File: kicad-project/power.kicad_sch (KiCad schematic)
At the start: 18 parts

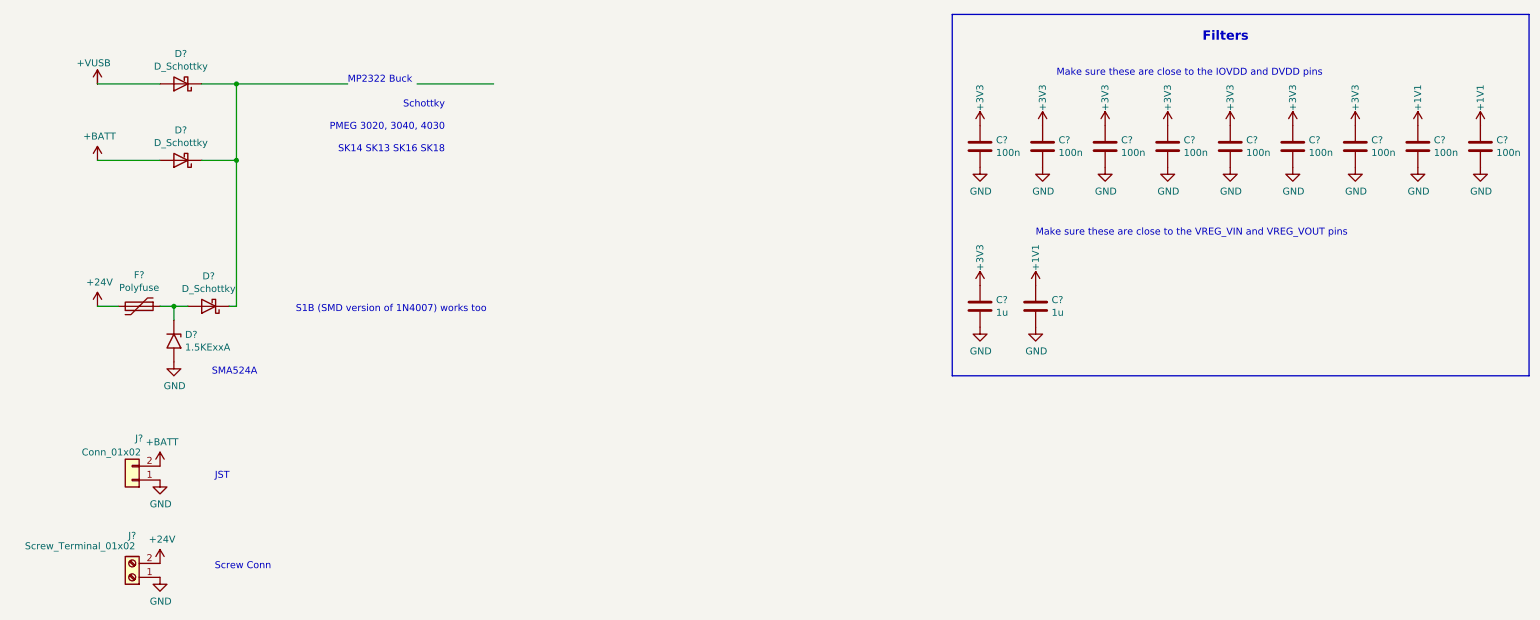
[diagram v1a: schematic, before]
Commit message: hw: add flash, switching circuit and XOUT resistor, change GPS and general cleanup
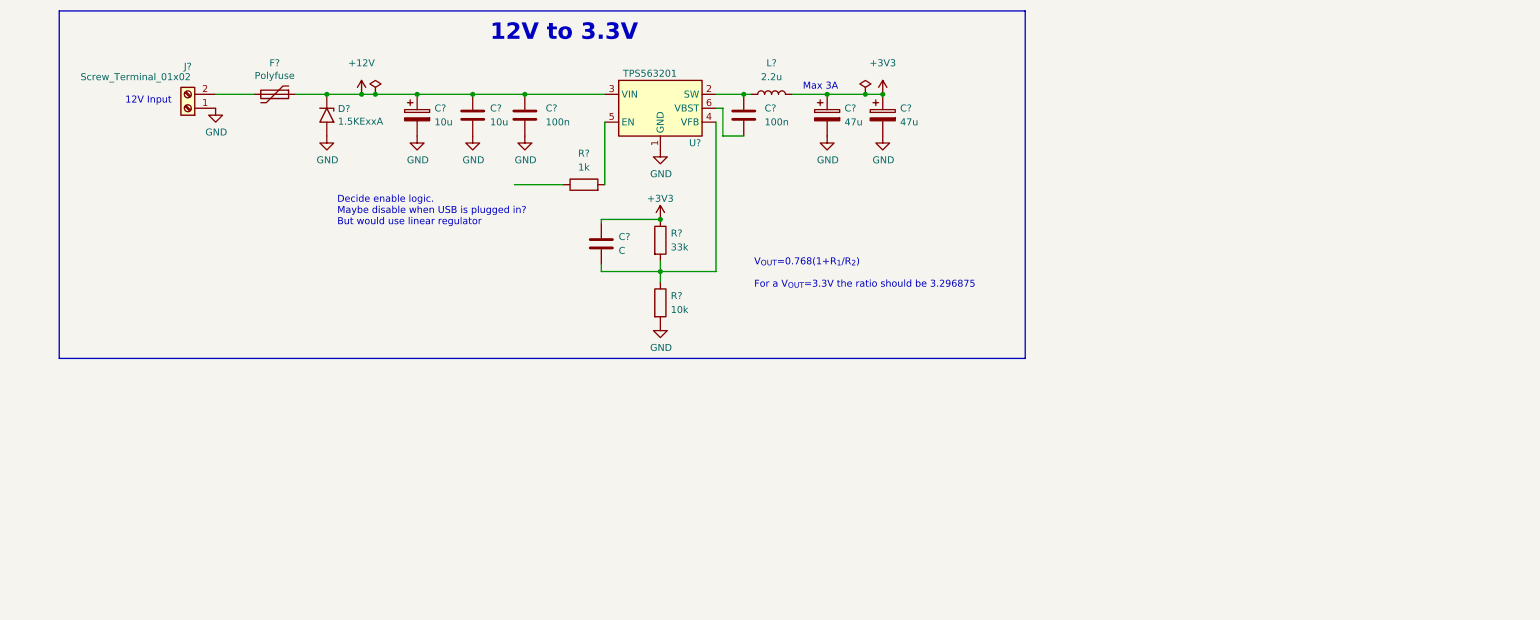
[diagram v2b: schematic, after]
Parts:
- removed C? (x9): 100n, Capacitor_SMD:C_0603_1608Metric, symbol Device:C
- removed C? (x2): 1u, Capacitor_SMD:C_0603_1608Metric, symbol Device:C
- removed D? (x3): D_Schottky, symbol Device:D_Schottky
- removed J?: Conn_01x02, symbol Connector_Generic:Conn_01x02
- added C?: 10u, symbol Device:C_Polarized
- added C?: C, symbol Device:C
- added C? (x2): 47u, symbol Device:C_Polarized
- added C? (x2): 100n, symbol Device:C
- added C?: 10u, symbol Device:C
- added L?: 2.2u, symbol Device:L
- added R?: 33k, symbol Device:R
- added R?: 10k, symbol Device:R
- added R?: 1k, symbol Device:R
- added U?: TPS563201, Package_TO_SOT_SMD:SOT-23-6, symbol Regulator_Switching:TPS563200
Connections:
- net +3V3: now also C?.1, C?.1, C?.1, L?.2, R?.1
- net GND: now also C?.2, C?.2, C?.2, C?.2, C?.2, R?.2, U?.1 (GND)
- net +12V: now reaches D?.1 (A1), F?.1
- net +12V: now also C?.1, C?.1, C?.1, U?.3 (VIN)
- net +24V: no longer names the net of F?.2, J?.2 (Pin_2)
- new net: C?.2, R?.1, R?.2, U?.4 (VFB)
- new net: C?.1, L?.1, U?.2 (SW)
- new net: R?.2, U?.5 (EN)
- new net: C?.2, U?.6 (VBST)
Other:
- note added: "12V Input"
- note added: "12V to 3.3V"
- note added: "Decide enable logic. Maybe disable when USB is plugged in? But would use linear regulator"
- note added: "Max 3A"
- note added: "V_{OUT}=0.768(1+R_{1}/R_{2}) For a V_{OUT}=3.3V the ratio should be 3.296875"
- note removed: "Filters"
- note removed: "JST"
- note removed: "MP2322 Buck"
- note removed: "Make sure these are close to the IOVDD and DVDD pins"
- note removed: "Make sure these are close to the VREG_VIN and VREG_VOUT pins"
- note removed: "S1B (SMD version of 1N4007) works too"
- note removed: "SMA524A"
- note removed: "Schottky PMEG 3020, 3040, 4030 SK14 SK13 SK16 SK18"
- note removed: "Screw Conn"
- title: (none) -> Power
- moved on the sheet: D?, F?, J?

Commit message: hw: add limit switches, dual power input, actuation sheet, debug and expansion connectors and connect sheets
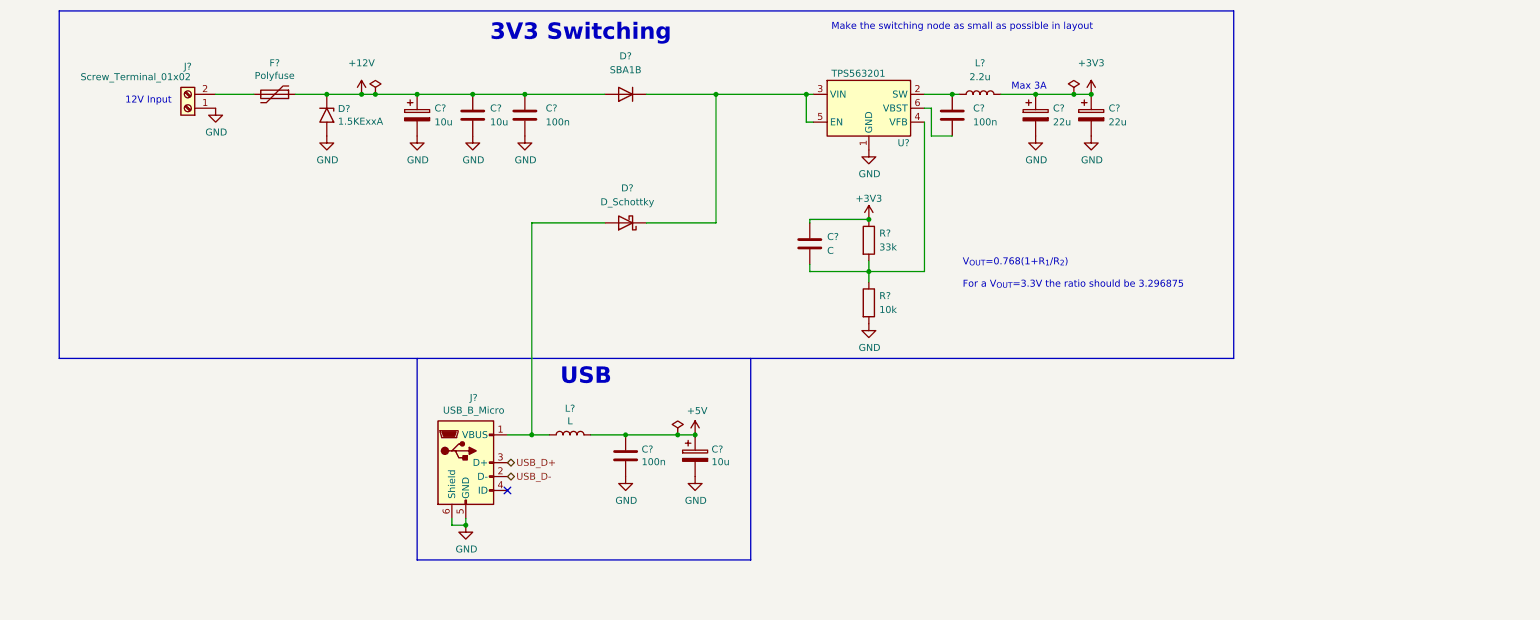
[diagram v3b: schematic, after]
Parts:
- removed R?: 1k, symbol Device:R
- added C?: 10u, symbol Device:CP
- added C?: 100n, symbol Device:C
- added D?: SBA1B, symbol Diode:1N4007
- added D?: D_Schottky, symbol Device:D_Schottky
- added J?: USB_B_Micro, symbol Connector:USB_B_Micro
- added L?: L, symbol Device:L
- C? (x2): value 47u -> 22u
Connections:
- net +12V: now also D?.2 (A); no longer U?.3 (VIN)
- net GND: now also C?.2, C?.2, J?.5 (GND), J?.6 (Shield)
- net at U?.5 (EN): now also U?.3 (VIN), D?.1 (K), D?.1 (K)
- new net: D?.2 (A), J?.1 (VBUS), L?.1
- new net +5V: C?.1, C?.1, L?.2
- new net USB_D+: J?.3 (D+)
- new net USB_D-: J?.2 (D-)
- no-connect marks 0 -> 1
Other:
- note added: "3V3 Switching"
- note added: "Make the switching node as small as possible in layout"
- note added: "USB"
- note removed: "12V to 3.3V"
- note removed: "Decide enable logic. Maybe disable when USB is plugged in? But would use linear regulator"
- moved on the sheet: C?, L?, R?, U?

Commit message: hw: schematic updates
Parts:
- removed C?: 10u, symbol Device:C
- added C? (x2): 10u, symbol Device:C_Polarized
- D?: value D_Schottky -> (none)
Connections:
- net +12V: now also C?.1
- net +5V: now also C?.1
- net GND: now also C?.2, C?.2
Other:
- note added: "How about no R in EN? 10k"
- note added: "S: Why not molex?"
- note added: "Why TVS here? Assuming 4x4.2 full charged LiPo/Li-Ion the diode should have 16.8V working voltage. We haven't found any TVS 16.8V."
- note added: "need motor current"
- note added: "perche 10 u polarizzati?"
- moved on the sheet: C?, D?, F?, J?, L?, R?, U?

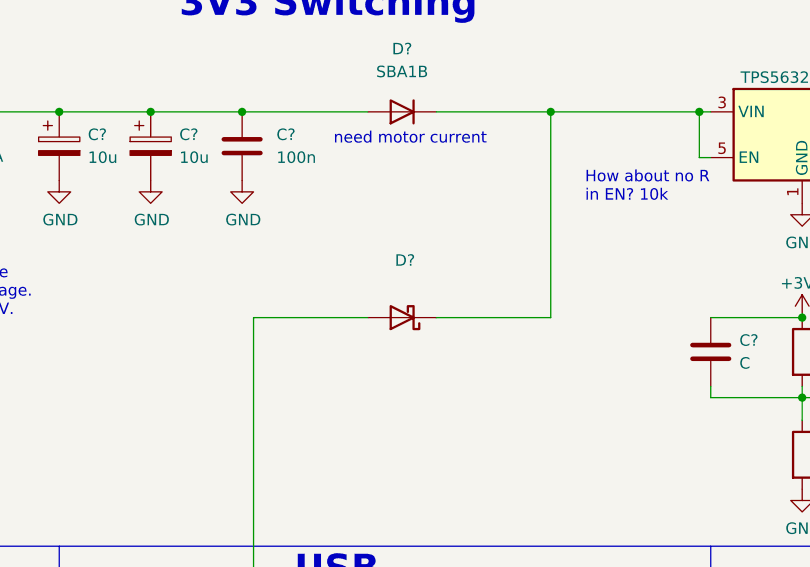
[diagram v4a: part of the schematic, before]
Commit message: hw: connect filtering capacitor near vdd pin
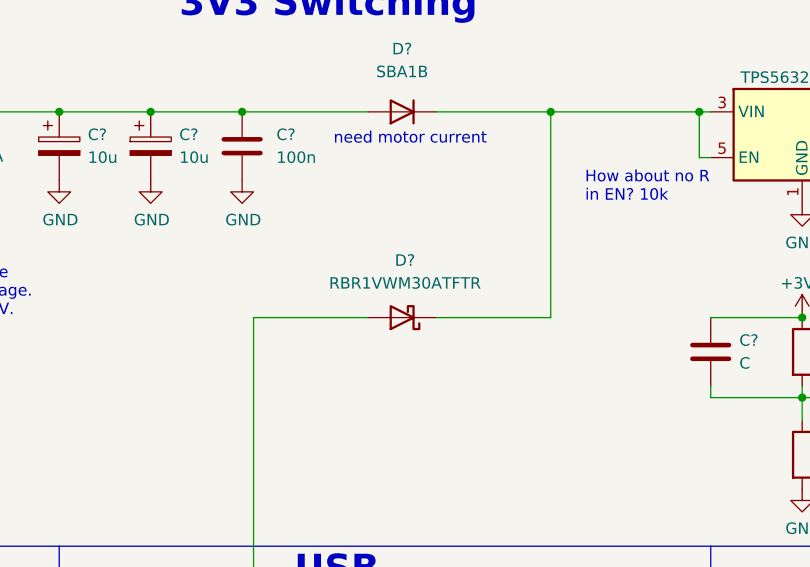
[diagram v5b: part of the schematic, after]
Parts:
- D?: value (none) -> RBR1VWM30ATFTR
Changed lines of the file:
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@@
     (in_bom yes) (on_board yes) (fields_autoplaced)
     (property "Reference" "D?" (id 0) (at 117.1575 45.72 0))
-    (property "Value" "" (id 1) (at 117.1575 48.26 0))
+    (property "Value" "RBR1VWM30ATFTR" (id 1) (at 117.1575 48.26 0))
     (property "Footprint" "" (id 2) (at 116.84 52.07 0)
       (effects (font (size 1.27 1.27)) hide)

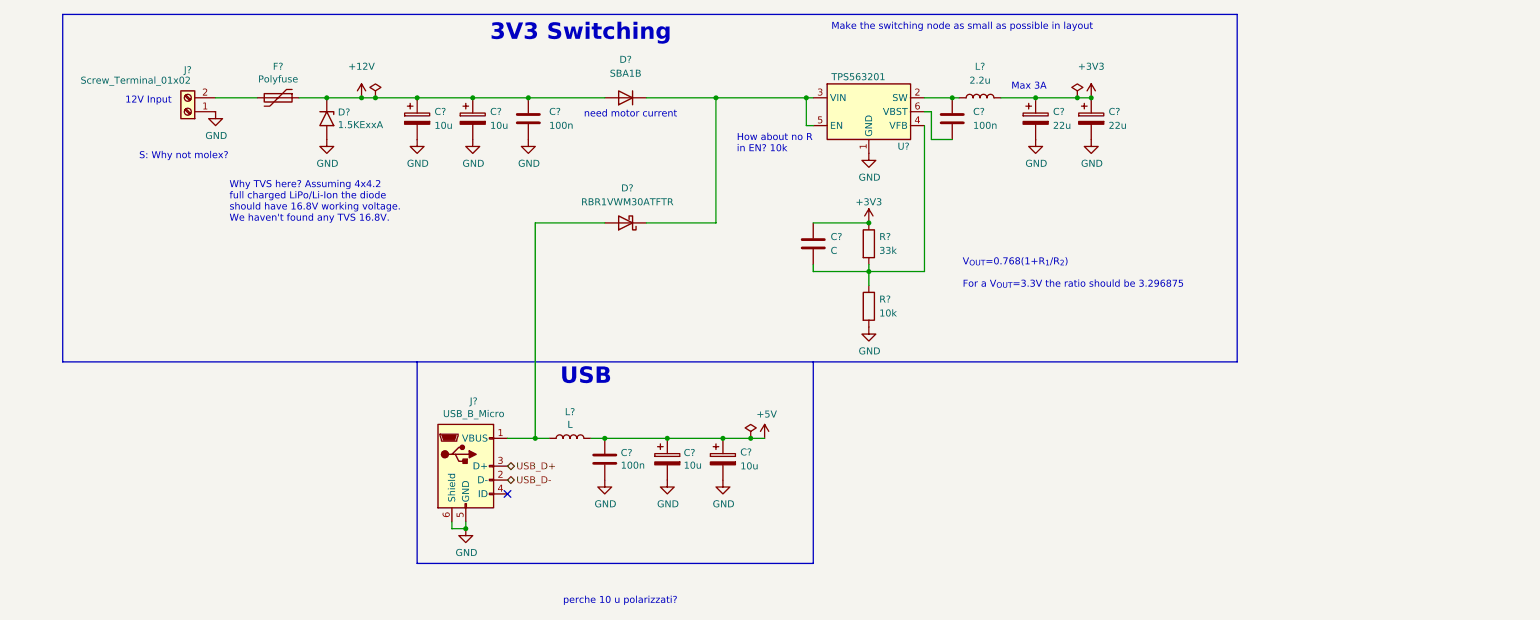
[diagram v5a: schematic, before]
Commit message: hw: update schematic pt. 2
add switching enable resistor, change usb inductor to ferrite bead, add OR gate and microstepping solder jumpers to motor driver, remove i2c and backup supply solder jumper from GPS, add ferrite bead to GPS, remove limit switches and other small changes
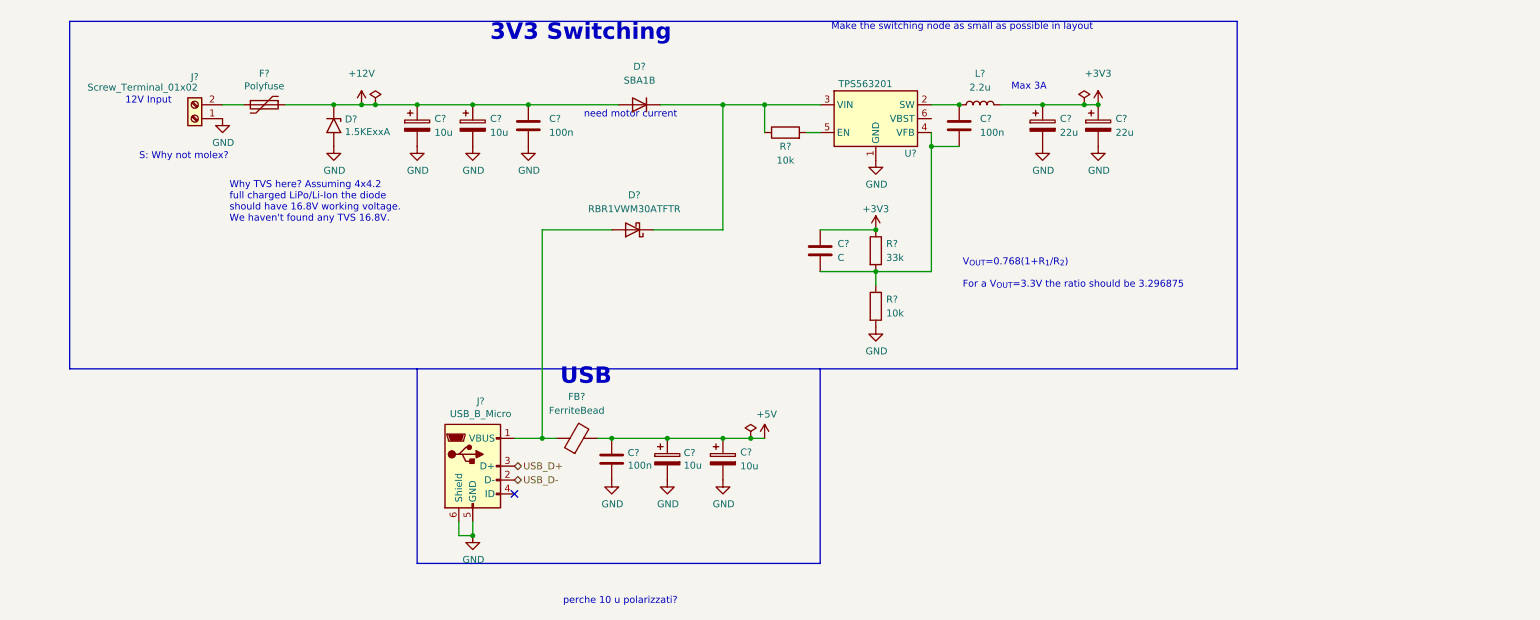
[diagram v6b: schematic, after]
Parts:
- removed L?: L, symbol Device:L
- added FB?: FerriteBead, symbol Device:FerriteBead
- added R?: 10k, symbol Device:R
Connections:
- net +5V: now also FB?.2
- net at C?.2, R?.1, R?.2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: now also C?.2
- net at D?.1 (K), D?.1 (K), U?.3 (VIN): now also R?.1; no longer U?.5 (EN)
- net at D?.2 (A), J?.1 (VBUS): now also FB?.1
- net at U?.6 (VBST): no longer C?.2
- new net: R?.2, U?.5 (EN)
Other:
- note removed: "How about no R in EN? 10k"
- moved on the sheet: C?, D?, F?, J?, L?, R?, U?

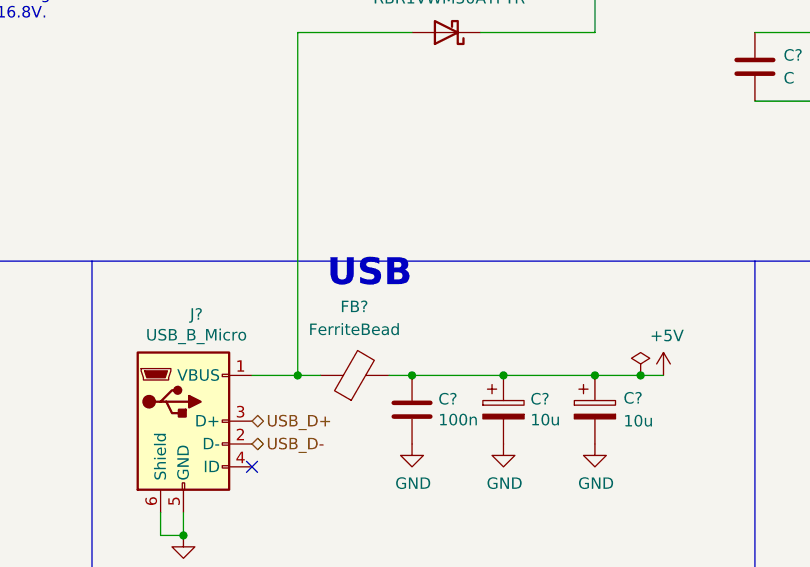
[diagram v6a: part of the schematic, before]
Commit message: hw: added MAN_NORD and TRCK_ON_OFF buttons and OLED Display
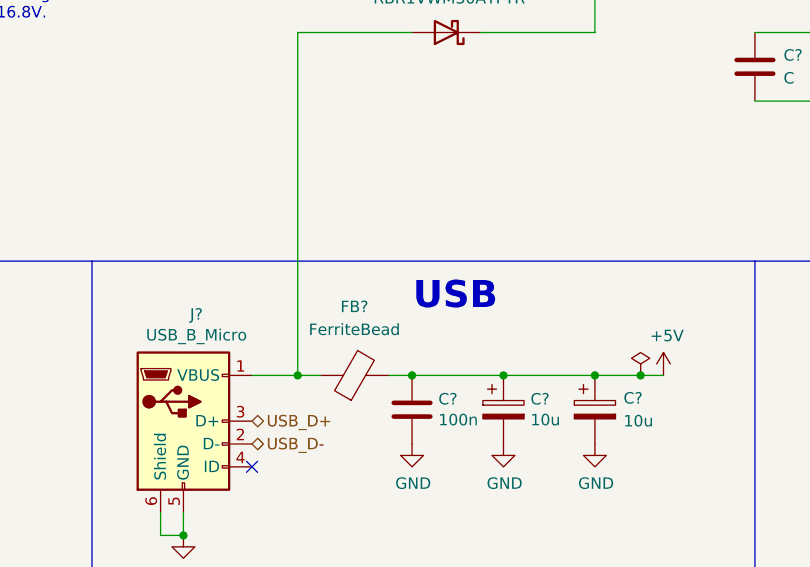
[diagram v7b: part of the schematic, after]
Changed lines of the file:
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@@
     (effects (font (size 1.27 1.27)) (justify left bottom))
   )
-  (text "USB" (at 114.3 81.915 180)
+  (text "USB" (at 123.825 84.455 180)
     (effects (font (size 2.9972 2.9972) (thickness 0.5994) bold) (justify right bottom))
   )
